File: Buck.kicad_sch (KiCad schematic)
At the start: 18 parts, among them J8 Screw_Terminal_01x02, Q8 AO3401A, U7 MYRGC07506, U8 TLV707

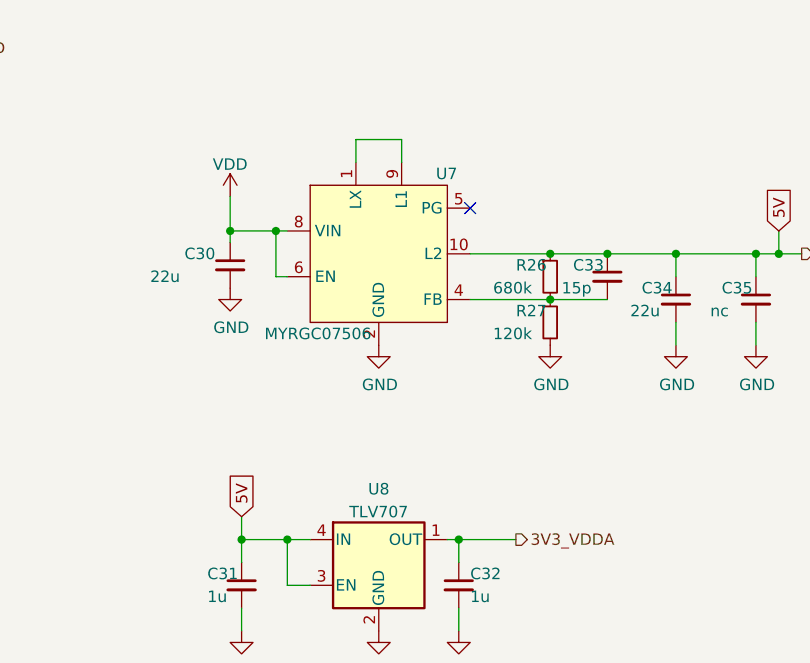
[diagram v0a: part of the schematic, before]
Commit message: added local symbol library
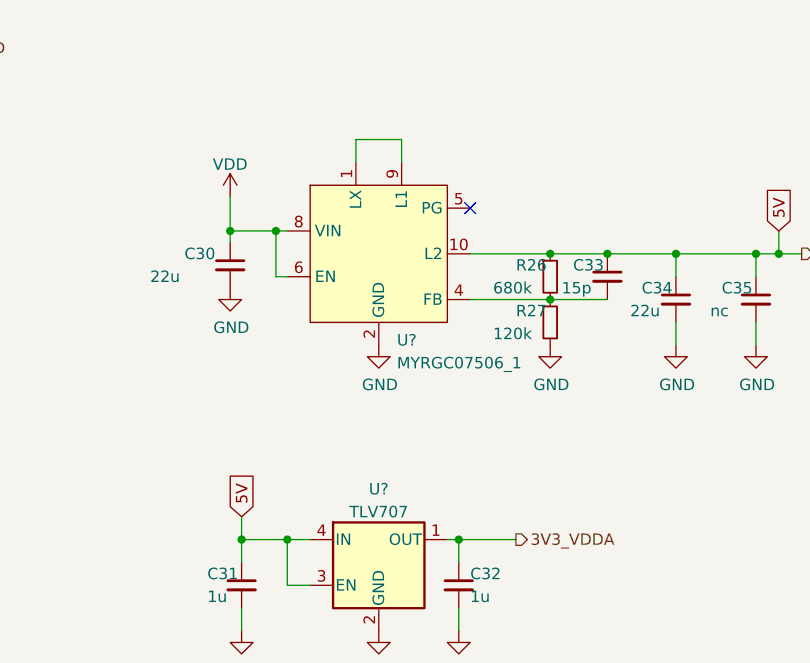
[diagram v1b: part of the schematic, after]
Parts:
- removed U7: MYRGC07506, symbol Mylibrary:MYRGC07506
- removed U8: TLV707, symbol Mylibrary:TLV707
- added U?: TLV707, symbol MyLibrary_PMSM:TLV707
- added U?: MYRGC07506_1, symbol MyLibrary_PMSM:MYRGC07506_1
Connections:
- net 3V3_VDDA: now also U?.1 (OUT)
- net 5V: now also U?.10 (L2), U?.3 (EN), U?.4 (IN)
- net GND: now also U?.2 (GND), U?.2 (GND)
- net VDD: now also U?.6 (EN), U?.8 (VIN)
- net at C33.2, R26.2, R27.1: now also U?.4 (FB)
- new net: U?.1 (LX), U?.9 (L1)

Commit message: Third commit
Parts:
- U7: renamed from U?; footprint (none) -> MyLibrary:Murata_picoBK
- U8: renamed from U?; footprint (none) -> MyLibrary:TLV707
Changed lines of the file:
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@@
   (symbol (lib_id "MyLibrary_PMSM:TLV707") (at 130.81 99.06 0) (unit 1)
     (in_bom yes) (on_board yes) (fields_autoplaced)
-    (property "Reference" "U?" (id 0) (at 130.81 90.9152 0))
+    (property "Reference" "U8" (id 0) (at 130.81 90.9152 0))
     (property "Value" "TLV707" (id 1) (at 130.81 93.4521 0))
-    (property "Footprint" "" (id 2) (at 130.81 90.805 0)
+    (property "Footprint" "MyLibrary:TLV707" (id 2) (at 130.81 90.805 0)
       (effects (font (size 1.27 1.27) italic) hide)
     )
@@
   (symbol (lib_id "MyLibrary_PMSM:MYRGC07506_1") (at 130.81 64.77 0) (unit 1)
     (in_bom yes) (on_board yes) (fields_autoplaced)
-    (property "Reference" "U?" (id 0) (at 132.8294 74.3696 0)
+    (property "Reference" "U7" (id 0) (at 132.8294 74.3696 0)
       (effects (font (size 1.27 1.27)) (justify left))
     )
@@
       (effects (font (size 1.27 1.27)) (justify left))
     )
-    (property "Footprint" "" (id 2) (at 147.32 77.47 0)
-      (effects (font (size 1.27 1.27)) hide)
-    )
+    (property "Footprint" "MyLibrary:Murata_picoBK" (id 2) (at 147.32 77.47 0)
+      (effects (font (size 1.27 1.27)) hide)
+    )

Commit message: added footprints
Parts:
- C26, C27, C28, C29: footprint (none) -> Capacitor_SMD:CP_Elec_10x12.6
- C30: footprint (none) -> Capacitor_SMD:C_0805_2012Metric
- C31, C32, C33, C34, C35: footprint (none) -> Capacitor_SMD:C_0603_1608Metric
- D5: footprint (none) -> Diode_SMD:D_SOD-323
- R26, R27: footprint (none) -> Resistor_SMD:R_0603_1608Metric
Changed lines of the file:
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@@
       (effects (font (size 1.27 1.27)) (justify left))
     )
-    (property "Footprint" "" (id 2) (at 114.3 66.04 0)
+    (property "Footprint" "Capacitor_SMD:C_0805_2012Metric" (id 2) (at 114.3 66.04 0)
       (effects (font (size 1.27 1.27)) hide)
     )
@@
       (effects (font (size 1.27 1.27)) (justify left))
     )
-    (property "Footprint" "" (id 2) (at 149.86 67.31 0)
+    (property "Footprint" "Resistor_SMD:R_0603_1608Metric" (id 2) (at 149.86 67.31 0)
       (effects (font (size 1.27 1.27)) hide)
     )
@@
       (effects (font (size 1.27 1.27)) (justify left))
     )
-    (property "Footprint" "" (id 2) (at 163.83 69.85 0)
+    (property "Footprint" "Capacitor_SMD:C_0603_1608Metric" (id 2) (at 163.83 69.85 0)
       (effects (font (size 1.27 1.27)) hide)
     )
@@
       (effects (font (size 1.27 1.27)) (justify left))
     )
-    (property "Footprint" "" (id 2) (at 45.72 101.6 0)
+    (property "Footprint" "Capacitor_SMD:CP_Elec_10x12.6" (id 2) (at 45.72 101.6 0)
       (effects (font (size 1.27 1.27)) hide)
     )
@@
       (effects (font (size 1.27 1.27)) (justify left))
     )
-    (property "Footprint" "" (id 2) (at 73.66 101.6 0)
+    (property "Footprint" "Capacitor_SMD:CP_Elec_10x12.6" (id 2) (at 73.66 101.6 0)
       (effects (font (size 1.27 1.27)) hide)
     )
@@
       (effects (font (size 1.27 1.27)) (justify left))
     )
-    (property "Footprint" "" (id 2) (at 139.7 101.6 0)
+    (property "Footprint" "Capacitor_SMD:C_0603_1608Metric" (id 2) (at 139.7 101.6 0)
       (effects (font (size 1.27 1.27)) hide)
     )
@@
       (effects (font (size 1.27 1.27)) (justify left))
     )
-    (property "Footprint" "" (id 2) (at 59.69 101.6 0)
+    (property "Footprint" "Capacitor_SMD:CP_Elec_10x12.6" (id 2) (at 59.69 101.6 0)
       (effects (font (size 1.27 1.27)) hide)
     )
@@
       (effects (font (size 1.27 1.27)) (justify left))
     )
-    (property "Footprint" "" (id 2) (at 31.75 101.6 0)
+    (property "Footprint" "Capacitor_SMD:CP_Elec_10x12.6" (id 2) (at 31.75 101.6 0)
       (effects (font (size 1.27 1.27)) hide)
     )
@@
       (effects (font (size 1.27 1.27)) (justify left))
     )
-    (property "Footprint" "" (id 2) (at 115.57 101.6 0)
+    (property "Footprint" "Capacitor_SMD:C_0603_1608Metric" (id 2) (at 115.57 101.6 0)
       (effects (font (size 1.27 1.27)) hide)
     )
@@
       (effects (font (size 1.27 1.27)) (justify left))
     )
-    (property "Footprint" "" (id 2) (at 172.72 69.85 0)
+    (property "Footprint" "Capacitor_SMD:C_0603_1608Metric" (id 2) (at 172.72 69.85 0)
       (effects (font (size 1.27 1.27)) hide)
     )
@@
       (effects (font (size 1.27 1.27)) (justify left))
     )
-    (property "Footprint" "" (id 2) (at 149.86 72.39 0)
+    (property "Footprint" "Resistor_SMD:R_0603_1608Metric" (id 2) (at 149.86 72.39 0)
       (effects (font (size 1.27 1.27)) hide)
     )
@@
       (effects (font (size 1.27 1.27)) (justify left))
     )
-    (property "Footprint" "" (id 2) (at 35.56 45.72 0)
+    (property "Footprint" "Diode_SMD:D_SOD-323" (id 2) (at 35.56 45.72 0)
       (effects (font (size 1.27 1.27)) hide)
     )
@@
       (effects (font (size 1.27 1.27)) (justify left))
     )
-    (property "Footprint" "" (id 2) (at 156.21 67.31 0)
-      (effects (font (size 1.27 1.27)) hide)
-    )
+    (property "Footprint" "Capacitor_SMD:C_0603_1608Metric" (id 2) (at 156.21 67.31 0)
+      (effects (font (size 1.27 1.27)) hide)
+    )

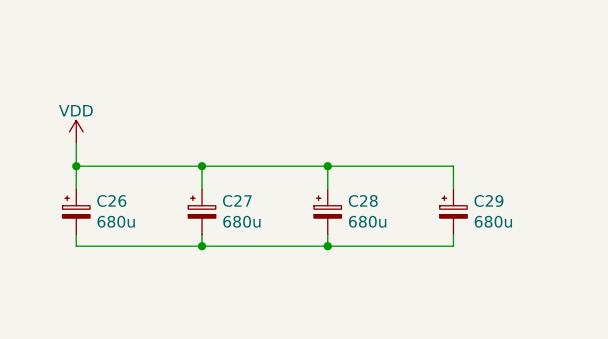
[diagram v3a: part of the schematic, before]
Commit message: started pcb layout
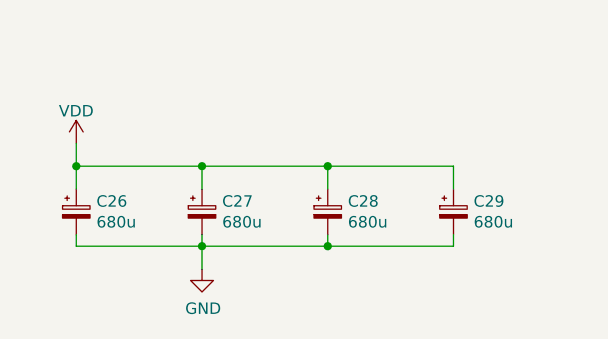
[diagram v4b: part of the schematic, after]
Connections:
- net GND: now also C26.2, C27.2, C28.2, C29.2
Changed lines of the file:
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@@
+    (stroke (width 0) (type default) (color 0 0 0 0))
+  )
+  (wire (pts (xy 45.72 105.41) (xy 45.72 107.95))
     (stroke (width 0) (type default) (color 0 0 0 0))
   )
@@
       (effects (font (size 1.27 1.27)) hide)
     )
+    (pin "1")
+  )
+  (symbol (lib_id "power:GND") (at 45.72 107.95 0) (unit 1)
+    (in_bom yes) (on_board yes)
+    (property "Reference" "#PWR036" (id 0) (at 45.72 114.3 0)
+      (effects (font (size 1.27 1.27)) hide)
+    )
+    (property "Value" "GND" (id 1) (at 45.847 112.3442 0))
+    (property "Footprint" "" (id 2) (at 45.72 107.95 0)
+      (effects (font (size 1.27 1.27)) hide)
+    )
+    (property "Datasheet" "" (id 3) (at 45.72 107.95 0)
+      (effects (font (size 1.27 1.27)) hide)
+    )

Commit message: added capacitor footprints
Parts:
- C26, C27, C28, C29: footprint Capacitor_SMD:CP_Elec_10x12.6 -> MyLibrary:Electrolytic_Cap_12.5x13.5
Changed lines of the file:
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@@
       (effects (font (size 1.27 1.27)) (justify left))
     )
-    (property "Footprint" "Capacitor_SMD:CP_Elec_10x12.6" (id 2) (at 45.72 101.6 0)
+    (property "Footprint" "MyLibrary:Electrolytic_Cap_12.5x13.5" (id 2) (at 45.72 101.6 0)
       (effects (font (size 1.27 1.27)) hide)
     )
@@
       (effects (font (size 1.27 1.27)) (justify left))
     )
-    (property "Footprint" "Capacitor_SMD:CP_Elec_10x12.6" (id 2) (at 73.66 101.6 0)
+    (property "Footprint" "MyLibrary:Electrolytic_Cap_12.5x13.5" (id 2) (at 73.66 101.6 0)
       (effects (font (size 1.27 1.27)) hide)
     )
@@
       (effects (font (size 1.27 1.27)) (justify left))
     )
-    (property "Footprint" "Capacitor_SMD:CP_Elec_10x12.6" (id 2) (at 59.69 101.6 0)
+    (property "Footprint" "MyLibrary:Electrolytic_Cap_12.5x13.5" (id 2) (at 59.69 101.6 0)
       (effects (font (size 1.27 1.27)) hide)
     )
@@
       (effects (font (size 1.27 1.27)) (justify left))
     )
-    (property "Footprint" "Capacitor_SMD:CP_Elec_10x12.6" (id 2) (at 31.75 101.6 0)
-      (effects (font (size 1.27 1.27)) hide)
-    )
+    (property "Footprint" "MyLibrary:Electrolytic_Cap_12.5x13.5" (id 2) (at 31.75 101.6 0)
+      (effects (font (size 1.27 1.27)) hide)
+    )

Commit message: rev_0.1
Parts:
- removed FB1: 600 @ 600MHz, Inductor_SMD:L_0805_2012Metric, symbol Device:Ferrite_Bead_Small
- removed Q8: AO3401A, Package_TO_SOT_SMD:SOT-23, symbol Transistor_FET:AO3401A
- added C36, C37: 1u, Capacitor_SMD:C_0603_1608Metric, symbol Device:C_Small
- added D6: UDZVFH10B, Diode_SMD:D_SOD-323_HandSoldering, symbol Device:D_Zener_Small
- added Q8: BSC022N04LSATMA1, MyLibrary:TDSON-8-6_copy, symbol MyLibrary:NMOS_Small
- added R28: 120k, Resistor_SMD:R_0603_1608Metric, symbol Device:R_Small
- added U9: TLV707, MyLibrary:TLV707, symbol MyLibrary_PMSM:TLV707
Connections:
- net V_SUPPLY is gone; now on net VDD: D5.1 (A1), J8.1 (Pin_1)
- net 5V: now also C36.1, U9.3 (EN), U9.4 (IN)
- net GND: now also C36.2, C37.2, D6.2 (A), Q8.3 (S), U9.2 (GND); no longer D5.2 (A2), J8.2 (Pin_2)
- net VDD: now also R28.1
- net FB: now reaches C33.2, R26.2, R27.1, U7.4 (FB)
- net LX: now reaches U7.1 (LX), U7.9 (L1)
- new net: D6.1 (K), Q8.2 (G), R28.2
- new net 3V3_MCU: C37.1, U9.1 (OUT)
- new net V_SUPPLY-: D5.2 (A2), J8.2 (Pin_2), Q8.1 (D)
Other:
- moved on the sheet: D5

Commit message: final
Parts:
- removed D5: D_TVS, Diode_SMD:D_SOD-323, symbol Device:D_TVS
- added Q9: AO3407A, Package_TO_SOT_SMD:SOT-23, symbol Transistor_FET:AO3401A
- added R37: 5.6k, Resistor_SMD:R_0603_1608Metric, symbol Device:R_Small
- added R38: 22k, Resistor_SMD:R_0603_1608Metric, symbol Device:R_Small
- added TP14, TP15, TP16, TP17, TP18: TestPoint, MyLibrary:TestPoint_1.0mm, symbol Connector:TestPoint
- added U11: LM258, Package_SO:SOIC-8_3.9x4.9mm_P1.27mm, symbol Amplifier_Operational:LM358
- C26, C27, C28, C29: Part (none) -> UCZ1V471MNQ1MS
- C30: footprint Capacitor_SMD:C_0805_2012Metric -> Capacitor_SMD:C_1206_3216Metric; Part (none) -> C3216X5R1V226M160AC
- C31, C32, C36, C37: Part (none) -> CL10B105KA8NNNC
- C33: Part (none) -> CL10C150JB8NNNC
- C34: Part (none) -> CL10A226MQ8NRNC
- D6: Part (none) -> UDZVFH10B --------
- Q8: value BSC022N04LSATMA1 -> BSC010N04LSATMA1; Part (none) -> BSC010N04LSATMA1
- U7: Part (none) -> MYRGC07506
- U8, U9: Part (none) -> TLV70733DQNT
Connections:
- net 3V3_MCU: now also TP18.1
- net 3V3_VDDA: now also TP17.1
- net 5V: now also TP16.1
- net FB: now also TP15.1
- net GND: now also R38.1, U11.4 (V-)
- net VDD: now also R37.2
- new net +5V: Q9.2 (S), U11.2 (-), U11.5 (+), U11.8 (V+)
- new net 5V_VBUS: Q9.3 (D)
- new net UNUSED: U11.6 (-), U11.7
- new net Vcomp+: R37.1, R38.2, TP14.1, U11.3 (+)
- new net Vusb_En: Q9.1 (G), U11.1
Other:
- moved on the sheet: C30, C33, C34, C35, R26, R27, U7

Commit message: last commit
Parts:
- R26: Part (none) -> RC0603FR-07680KL
- R27, R28: Part (none) -> AC0603FR-07120KL
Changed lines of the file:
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@@
+      (effects (font (size 1.27 1.27)) hide)
+    )
+    (property "Part" "AC0603FR-07120KL" (id 4) (at 129.032 61.976 0)
       (effects (font (size 1.27 1.27)) hide)
     )
@@
       (effects (font (size 1.27 1.27)) hide)
     )
+    (property "Part" "RC0603FR-07680KL" (id 4) (at 129.032 56.896 0)
+      (effects (font (size 1.27 1.27)) hide)
+    )
     (pin "1")
     (pin "2")
@@
       (effects (font (size 1.27 1.27)) hide)
     )
+    (property "Part" "AC0603FR-07120KL" (id 4) (at 46.355 45.085 0)
+      (effects (font (size 1.27 1.27)) hide)
+    )
